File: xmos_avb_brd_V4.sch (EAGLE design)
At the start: 139 parts, among them IC1 IS25LP080D-JULE-TR_IS25LP080D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, J1 0826-1X1T-KL-F_0826-1X1T-KL-F, U1 AG9900_AG9905LP, U10 ST-MICROELECTRONICS2_ST1S06PUR, U2 AR8035_AR8035-AL1A-R, U3 XE216-512-TQ128-C20_XE216-512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, U4 ADM1085AKSZ-REEL7_ADM1085AKSZ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, U5 NC7WZ07P6X_NC7WZ07P6X, U6 CS2100-CP_CS2100-CP-CZZ, U7 ST-MICROELECTRONICS2_ST1S06PUR, U8 NCP303LSN30, U9 MIC5213-2.5V, X1 FA-238 25.000, X2 TC2050-XTAG_TC2050-NL-MCP-NL, X3 CON-MOLEX_52559-3092, X4 CON-MOLEX_52559-0692, Y1 ECS-3225Q-33-240-DP-TR_ECS-32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

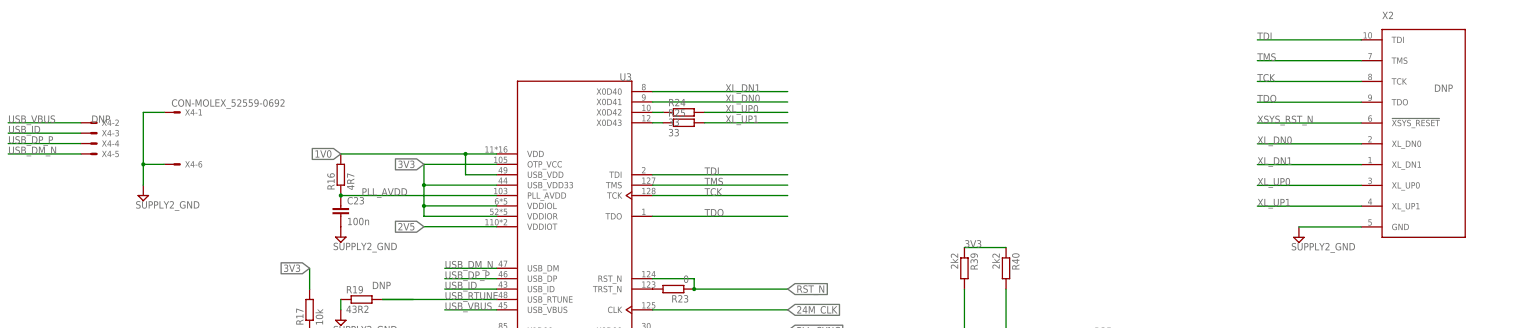
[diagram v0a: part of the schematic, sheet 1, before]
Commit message: new debug header added to improve debugging with xmos. old tag-connect removed.
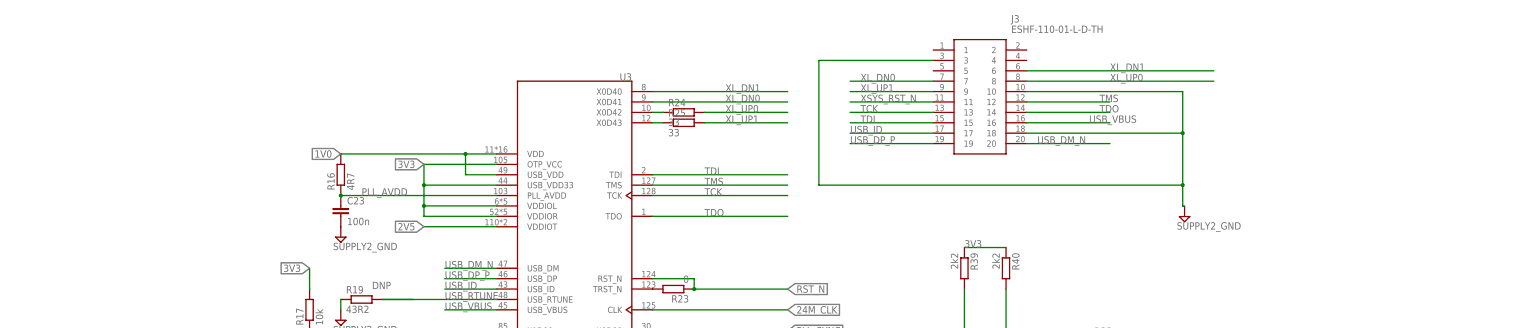
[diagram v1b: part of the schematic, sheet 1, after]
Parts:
- removed X2: TC2050-XTAG_TC2050-NL-MCP-NL, xmos_avb_brd_V4:TC2050-XTAG_TC2050-NL-MCP-NL
- removed X4: CON-MOLEX_52559-0692, xmos_avb_brd_V4:CON-MOLEX_52559-0692
- added C30, C56, C57, C58: 1u, xmos_avb_brd_V4:RCL_C-EUC1206
- added IC3: KSZ9131RNXI-TR, KSZ9131RNXI-TR:KSZ9131RNXI-TR
- added J3: ESHF-110-01-L-D-TH, ESHF-110-01-L-D-TH:ESHF-110-01-L-D-TH
- C9: value EEH-ZC1V101P_EEH-ZC1V101P -> 1u; device xmos_avb_brd_V4:EEH-ZC1V101P_EEH-ZC1V101P -> xmos_avb_brd_V4:RCL_C-EUC1206
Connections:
- net GND: now also C30.2, C56.2, C57.2, C58.2, C9.2, J3.10, J3.18, J3.3; no longer C9.-, X2.GND, X4-1.S, X4-6.S
- net TCK: now also J3.13; no longer X2.TCK
- net TDI: now also J3.15; no longer X2.TDI
- net TDO: now also J3.14; no longer X2.TDO
- net TMS: now also J3.12; no longer X2.TMS
- net USB_DM_N: now also J3.20; no longer X4-5.S
- net USB_DP_P: now also J3.19; no longer X4-4.S
- net USB_ID: now also J3.17; no longer X4-3.S
- net USB_VBUS: now also J3.16; no longer X4-2.S
- net VDC: now also C30.1, C56.1, C57.1, C58.1, C9.1; no longer C9.+
- net XL_DN0: now also J3.7; no longer X2.XL_DN0
- net XL_DN1: now also J3.6; no longer X2.XL_DN1
- net XL_UP0: now also J3.8; no longer X2.XL_UP0
- net XL_UP1: now also J3.9; no longer X2.XL_UP1
- net XSYS_RST_N: now also J3.11; no longer X2.!XSYS_RESET
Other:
- moved on the sheet: FL2

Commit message: ksz9131 added to schematic.#
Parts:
- removed C16: 100n, xmos_avb_brd_V4:RCL_C-EUC0402
- removed C18, C19: 1u, xmos_avb_brd_V4:RCL_C-EUC1206
- removed L1: 4u7, xmos_avb_brd_V4:RCL_L-EUL2012C
- removed U2: AR8035_AR8035-AL1A-R, xmos_avb_brd_V4:AR8035_AR8035-AL1A-R
- added C59, C60, C64, C65, C69, C71, C72, C73: 100n, xmos_avb_brd_V4:RCL_C-EUC0402
- added C61, C62, C63, C66, C67, C68, C70: 10u, xmos_avb_brd_V4:RCL_C-EUC1206
- added FL5, FL6, FL7: BLM21AG471SN1D_BLM21AG471SN1D, xmos_avb_brd_V4:BLM21AG471SN1D_BLM21AG471SN1D
- added IC4: DMP2004K-7, DMP2004K-7:DMP2004K-7
- added R57: 4R7, xmos_avb_brd_V4:RCL_R-EU_R0402
- added R58: 6k04, xmos_avb_brd_V4:RCL_R-EU_R0402
- added R59: 100k, xmos_avb_brd_V4:RCL_R-EU_R0402
- added R60: 10k, xmos_avb_brd_V4:RCL_R-EU_R0402
- added R61: 4k7, xmos_avb_brd_V4:RCL_R-EU_R0402
- C11: value 10u -> 100n; device xmos_avb_brd_V4:RCL_C-EUC1206 -> xmos_avb_brd_V4:RCL_C-EUC0402
- C12: value 100n -> 10u; device xmos_avb_brd_V4:RCL_C-EUC0402 -> xmos_avb_brd_V4:RCL_C-EUC1206
- C5, C6, C7: value 470p -> 100n
- R10, R6, R7: value 10k -> 1k
- R11: value 2k37 -> 10k
- R15: value 1k5 -> 1k
- R5: value 510 -> 10k
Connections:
- removed net 1V1: C11.1, C14.1, C17.1, FL1.1, L1.2, U2.DVDDL
- removed net AVDD33: C13.1, C18.1, FL3.2, U2.AVDD33
- removed net VDDH_REG: C16.1, C19.1, R10.2, R13.2, R14.2, R15.2, R6.2, R7.2, U2.VDDH_REG, U2.VDDIO_REG
- new net N$11: C59.1, FL5.1, IC3.AVDDL_PLL
- new net N$12: FL1.1
- new net N$17: C13.1, C60.1, C61.1, C62.1, C63.1, FL3.2, IC3.AVDDH_1, IC3.AVDDH_2, IC4.S, R59.1
- new net N$27: C17.1, C64.1, C65.1, C66.1, C67.1, C68.1, FL6.2, IC3.DVDDH_1, IC3.DVDDH_2, IC3.DVDDH_3
- new net N$31: IC3.ISET, R58.1
- new net N$32: IC4.G, R57.1, R59.2
- new net PHY_DVDDH: C7.1, R10.2, R11.2, R13.2, R14.2, R15.2, R5.2, R61.2
- new net PHY_VDD: C69.1, C70.1, C71.1, FL3.1, FL6.1
- new net PWR: C10.1, C11.1, C14.1, C72.1, C73.1, C8.1, FL7.1, IC3.DVDDL_1, IC3.DVDDL_2, IC3.DVDDL_3, IC3.DVDDL_4, IC3.DVDDL_5
- net 3V3: no longer C10.1, C8.1, FL3.1, R5.2, U2.VDD33
- net AVDDL: now also FL5.2, FL7.2, IC3.AVDDL_1, IC3.AVDDL_2, IC4.D; no longer U2.AVDDL@1, U2.AVDDL@2, U2.AVDDL@3
- net GND: now also C59.2, IC3.P_VSS, IC3.VSS, R58.2, R6.1, R60.1, R7.1; no longer C11.2, C12.2, C13.2, C14.2, C16.2, C18.2, C19.2, C7.2, R11.1, U2.GND
- net N$10: now also IC3.XI; no longer U2.XTLI
- net N$13: now also IC3.RXC/PHYAD2; no longer U2.RX_CLK
- net N$14: now also IC3.LED1/PME_N1//PHYAD0, R7.2; no longer C7.1, R10.1, U2.LED_ACT
- net N$20: now also IC3.CLK125_NDO/LED_MODE, R5.1; no longer R11.2, U2.RBIAS
- net N$3: now also IC3.LDO_O, R57.2; no longer L1.1, U2.LX
- net N$54: now also IC3.LED2/PHYAD1, R6.2; no longer C5.1, R5.1, R6.1, U2.LED_1000
- net N$6: no longer R7.1, U2.LED_10_100
- net N$8: now also C5.1
- net N$9: now also IC3.XO; no longer U2.XTLO
- net PHY_INT: now also IC3.INT_N/PME_N2/ALLPHYAD, R61.1; no longer U2.INT
- net PHY_MDC: now also IC3.MDC, R10.1; no longer U2.MDC
- net PHY_MDIO: now also IC3.MDIO; no longer U2.MDIO
- net PHY_RSTN: now also IC3.RESET_N; no longer U2.RSTN
- net RX_D0: now also IC3.RXD0/MODE0, R60.2; no longer U2.RXD0
- net RX_D1: now also IC3.RXD1/MODE1, R13.1; no longer U2.RXD1
- net RX_D2: now also IC3.RXD2/MODE2, R14.1; no longer R13.1, U2.RXD2
- net RX_D3: now also IC3.RXD3/MODE3, R11.1; no longer R14.1, U2.RXD3
- net RX_DV: now also IC3.RX_CTL/CLK125_EN; no longer U2.RX_DV
- net TRD1_N: now also IC3.TXRXM_A; no longer U2.TRXN0
- net TRD1_P: now also IC3.TXRXP_A; no longer U2.TRXP0
- net TRD2_N: now also IC3.TXRXM_B; no longer U2.TRXN1
- net TRD2_P: now also IC3.TXRXP_B; no longer U2.TRXP1
- net TRD3_N: now also IC3.TXRXM_C; no longer U2.TRXN2
- net TRD3_P: now also IC3.TXRXP_C; no longer U2.TRXP2
- net TRD4_N: now also IC3.TXRXM_D; no longer U2.TRXN3
- net TRD4_P: now also IC3.TXRXP_D; no longer U2.TRXP3
- net TX_CLK: now also IC3.TXC; no longer U2.GTX_CLK
- net TX_D0: now also IC3.TXD0; no longer U2.TXD0
- net TX_D1: now also IC3.TXD1; no longer U2.TXD1
- net TX_D2: now also IC3.TXD2; no longer U2.TXD2
- net TX_D3: now also IC3.TXD3; no longer U2.TXD3
- net TX_EN: now also IC3.TX_CTL; no longer U2.TX_EN
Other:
- note removed: "only one of both outputs is active - see datasheet p. 13"
- moved on the sheet: C1, C10, C11, C12, C13, C14, C15, C17, C2, C20, C21, C22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

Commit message: layout wip
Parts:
- removed C52, C54, C57: 1u, xmos_avb_brd_V4:RCL_C-EUC1206
- removed C70: 10u, xmos_avb_brd_V4:RCL_C-EUC1206
- removed FL1: BLM21AG471SN1D_BLM21AG471SN1D, xmos_avb_brd_V4:BLM21AG471SN1D_BLM21AG471SN1D
- removed U9: MIC5213-2.5V, xmos_avb_brd_V4:MICREL2_MIC5213
- added C16, C18, C19: 10u, xmos_avb_brd_V4:RCL_C-EUC1206
- C30: value 1u -> 100n; device xmos_avb_brd_V4:RCL_C-EUC1206 -> xmos_avb_brd_V4:RCL_C-EUC0402
- C32, C53: value 4u7 -> 10u
- C46, C55: value 22u -> 10u
- C56, C58, C9: value 1u -> 10u
- FL3, FL5, FL6, FL7: value BLM21AG471SN1D_BLM21AG471SN1D -> 742792711; device xmos_avb_brd_V4:BLM21AG471SN1D_BLM21AG471SN1D -> 742792711:742792711
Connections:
- net N$11 renamed AVDDL_PLL
- net N$17 renamed AVDDH
- net N$3 renamed LDO
- net PWR renamed DVDDL
- removed net 2V5: C33.1, C54.1, U3.VDDIOT, U9.OUT
- removed net N$12: FL1.1
- removed net N$27: C17.1, C64.1, C65.1, C66.1, C67.1, C68.1, FL6.2, IC3.DVDDH_1, IC3.DVDDH_2, IC3.DVDDH_3
- removed net PHY_DVDDH: C7.1, R10.2, R11.2, R13.2, R14.2, R15.2, R5.2, R61.2
- removed net PHY_VDD: C69.1, C70.1, C71.1, FL3.1, FL6.1
- new net DVDDH: C17.1, C64.1, C65.1, C66.1, C67.1, C68.1, C7.1, FL6.2, IC3.DVDDH_1, IC3.DVDDH_2, IC3.DVDDH_3, R10.2, R11.2, R13.2, R14.2, R15.2, R5.2, R61.2
- new net PHY_VDD_3V3: C33.1, C69.1, C71.1, FL3.1, FL6.1, U3.VDDIOT
- net 1V0: now also C19.1
- net 3V3: now also C16.1, C18.1
- net 5V0: no longer C52.1, U9.EN, U9.IN
- net AVDDL: no longer FL1.2
- net GND: now also C11.2, C12.2, C13.2, C14.2, C16.2, C18.2, C19.2, C60.2, C61.2, C62.2, C63.2, C64.2, C65.2, C66.2, C67.2, C68.2, C69.2, C7.2, C71.2, C72.2, C73.2; no longer C30.2, C52.2, C54.2, C57.2, U9.GND
- net VDC: no longer C30.1, C57.1
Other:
- moved on the sheet: C10, C11, C14, C17, C30, C32, C34, C35, C36, C37, C38, C39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
